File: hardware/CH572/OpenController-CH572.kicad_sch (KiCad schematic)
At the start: 9 parts, among them J1 Castellated, U1 CH572D, U2 XC6206P332MR-G, Y1 32MHz

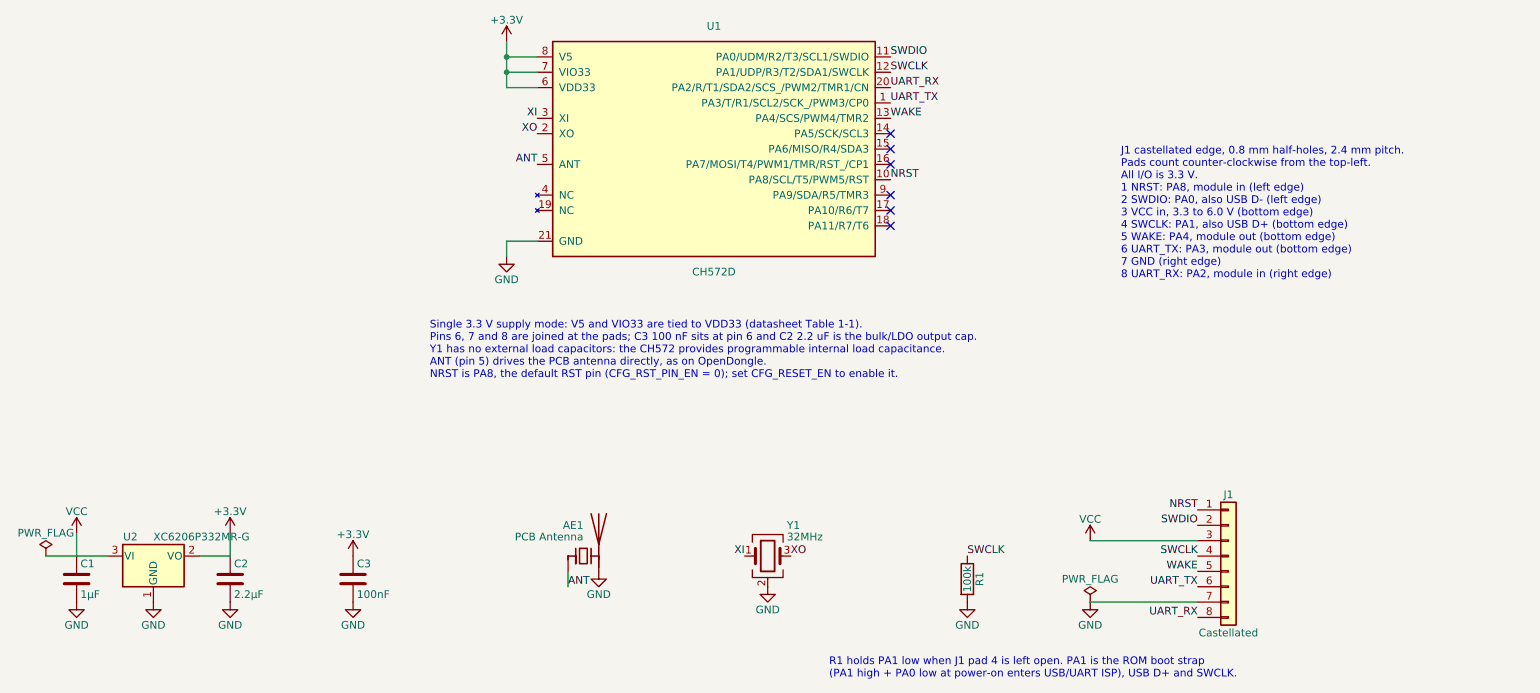
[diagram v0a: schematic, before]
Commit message: hardware: move the CH572 castellations to a 0.1 in grid
Nine castellated half-holes (1.0 mm drill, 1.5 x 3.0 mm pads) replace the
eight on a 2.4 mm pitch: three on each side and three on the end opposite
the antenna, all on one 0.1 in grid so a host can also take standard pin
headers. The board widens from 10.0 mm to 10.16 mm so the side rows sit
0.4 in apart; the antenna stays centred. Viewed from the top with the
antenna at the bottom, the pads count counter-clockwise from the
top-left: 1 GND, 2 UART_TX, 3 UART_RX, 4 NRST, 5 VCC, 6 GND, 7 SWDIO,
8 SWCLK, 9 WAKE.

The board is now drawn with the antenna at the bottom (rotated 180
degrees). Besides the new J1 footprint and the wider outline and pours,
the layout change re-points the six bottom-layer castellation runs and
the VCC run, moves C2 0.6 mm with its two tracks, moves two ground vias
clear of the new pads and adds two stitching vias beside the ground
castellations. The RF area is unchanged.

The outermost holes sit 2.54 mm from the corners, which clears
JLCPCB's 1 mm castellated-pad-to-edge rule under both its English (pad
edge) and Chinese (hole edge) wording. Only the 3 mm hole-to-corner row
in the English design guide's expanded table is not met; the README
records why. ERC and DRC (with schematic parity) report no violations.

Co-Authored-By: Claude Opus 5.5 <noreply@anthropic.com>
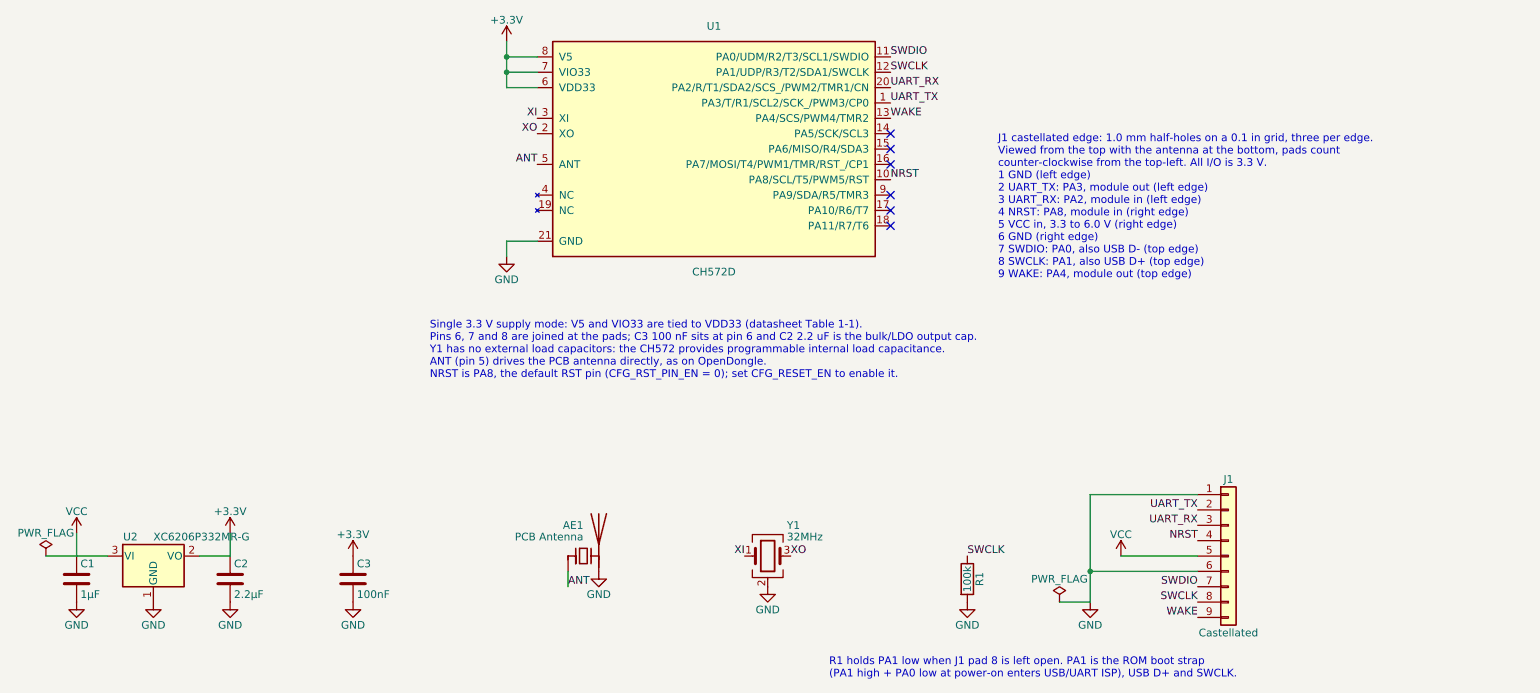
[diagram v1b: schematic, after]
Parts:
- J1: footprint OpenController:Castellated_CH572_10x20.5mm -> OpenController:Castellated_CH572_10.16x20.5mm; symbol Connector_Generic:Conn_01x08 -> Connector_Generic:Conn_01x09
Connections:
- net GND: now also J1.1 (Pin_1), J1.6 (Pin_6); no longer J1.7 (Pin_7)
- net NRST: now also J1.4 (Pin_4); no longer J1.1 (Pin_1)
- net SWCLK: now also J1.8 (Pin_8); no longer J1.4 (Pin_4)
- net SWDIO: now also J1.7 (Pin_7); no longer J1.2 (Pin_2)
- net UART_RX: now also J1.3 (Pin_3); no longer J1.8 (Pin_8)
- net UART_TX: now also J1.2 (Pin_2); no longer J1.6 (Pin_6)
- net VCC: now also J1.5 (Pin_5); no longer J1.3 (Pin_3)
- net WAKE: now also J1.9 (Pin_9); no longer J1.5 (Pin_5)
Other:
- note added: "J1 castellated edge: 1.0 mm half-holes on a 0.1 in grid, three per edge. Viewed from the top with the antenna at the bottom, pads count counter-clockwise from the top-left. All I/O is 3.3 V. 1 GND (left edge) 2 UART_TX: PA3, module out (left edge) 3 UART_RX: PA2, module in (left edge) 4 NRST: PA8, module in (right edge) 5 VCC in, 3.3 to 6.0 V (right edge) 6 GND (right edge) 7 SWDIO: PA0, also USB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"
- note added: "R1 holds PA1 low when J1 pad 8 is left open. PA1 is the ROM boot strap (PA1 high + PA0 low at power-on enters USB/UART ISP), USB D+ and SWCLK."
- note removed: "J1 castellated edge, 0.8 mm half-holes, 2.4 mm pitch. Pads count counter-clockwise from the top-left. All I/O is 3.3 V. 1 NRST: PA8, module in (left edge) 2 SWDIO: PA0, also USB D- (left edge) 3 VCC in, 3.3 to 6.0 V (bottom edge) 4 SWCLK: PA1, also USB D+ (bottom edge) 5 WAKE: PA4, module out (bottom edge) 6 UART_TX: PA3, module out (bottom edge) 7 GND (right edge) 8 UART_RX: PA2, module in (righ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"
- note removed: "R1 holds PA1 low when J1 pad 4 is left open. PA1 is the ROM boot strap (PA1 high + PA0 low at power-on enters USB/UART ISP), USB D+ and SWCLK."

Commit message: hardware: keep the CH572 exposed-pad paste off its thermal vias
The exposed pad's four 0.2 mm GND vias sat inside the footprint's 2 x 2
paste windows, so solder could wick into the open barrels during reflow
and starve the CH572D's only ground connection (CodeRabbit review).

U1 now uses a project copy of KiCad's QFN-20-1EP_3x3mm_P0.4mm_EP1.65x1.65mm
land pattern with four 0.4/0.2 mm thermal vias built in, 0.6 mm from the
centre along each axis. The paste is a central window plus four edge
windows covering about 47% of the pad, each at least 0.1 mm clear of the
via copper. The separate board vias in the pad are gone. ERC and DRC
(with schematic parity) report no violations.

Co-Authored-By: Claude Opus 5.5 <noreply@anthropic.com>
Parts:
- U1: footprint Package_DFN_QFN:QFN-20-1EP_3x3mm_P0.4mm_EP1.65x1.65mm -> OpenController:QFN-20-1EP_3x3mm_P0.4mm_EP1.65x1.65mm_ThermalVias
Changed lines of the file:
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@@
 			)
 		)
-		(property "Footprint" "Package_DFN_QFN:QFN-20-1EP_3x3mm_P0.4mm_EP1.65x1.65mm"
+		(property "Footprint" "OpenController:QFN-20-1EP_3x3mm_P0.4mm_EP1.65x1.65mm_ThermalVias"
 			(at 148.59 72.39 0)
 			(hide yes)

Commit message: hardware: draw the CH572D QFN footprint for OpenController
U1's thermal-via footprint was a modified copy of KiCad's
QFN-20-1EP_3x3mm_P0.4mm_EP1.65x1.65mm. KiCad's libraries are CC-BY-SA
4.0, and their exception does not cover library parts redistributed as
separate files, so that copy could not sit in a CERN-OHL-W project
library (Codex review).

The new footprint is drawn from scratch from the CH572 datasheet's QFN20
drawing (3.0 +/- 0.1 mm body, 1.8 +/- 0.2 mm exposed pad, 0.35 +/- 0.12
mm leads):
- lands 1.15 to 1.85 mm from the centre, 0.15 mm clear of the largest
  exposed pad;
- a 1.8 mm exposed-pad land with four 0.4/0.2 mm tented thermal vias at
  (+/-0.65, +/-0.65) mm;
- exposed-pad paste in a centre window plus four edge windows, 51% of
  the pad with their rounded corners and at least 0.09 mm clear of the
  via copper.
hardware/NOTICE records the footprint's provenance.

The README now quotes paste coverage including the windows' rounded
corners, and names the thermal vias (1.1 mm apart) rather than the
castellations as the closest plated pad holes. ERC and DRC (with
schematic parity) report no violations.

Co-Authored-By: Claude Opus 5.5 <noreply@anthropic.com>
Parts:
- U1: footprint OpenController:QFN-20-1EP_3x3mm_P0.4mm_EP1.65x1.65mm_ThermalVias -> OpenController:CH572D_QFN-20_3x3mm_P0.4mm_EP1.8mm_ThermalVias
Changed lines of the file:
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@@
 			)
 		)
-		(property "Footprint" "OpenController:QFN-20-1EP_3x3mm_P0.4mm_EP1.65x1.65mm_ThermalVias"
+		(property "Footprint" "OpenController:CH572D_QFN-20_3x3mm_P0.4mm_EP1.8mm_ThermalVias"
 			(at 148.59 72.39 0)
 			(hide yes)
